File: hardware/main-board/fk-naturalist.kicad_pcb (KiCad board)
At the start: 2 copper layers, 91.8 x 37 mm, 128 parts, among them J1 Conn_01x07, J10 S2B-PH-SM4-TB, J11 RF-SMA-EDGE, J4 Conn_01x02, J5 Conn_01x03, J6 Conn_01x05, J7 CONN-HDR-2x5, J8 Conn_01x09, J9 MICRO-USB, M1 MOUNT_HOLE, M2 FIDUCIAL, M3 MOUNT_HOLE, M4 MOUNT_HOLE, M5 FIDUCIAL, M6 MOUNT_HOLE, M7 MICROSD, M8 FIDUCIAL, Q1 2N7002LT1G, Q2 2N7002LT1G, Q3 2N7002LT1G, Q4 2N7002LT1G, Q5 2N7002LT1G, SW1 SPNO, SW2 SPNO, U1 ATWINC1500-MR210PA, U10 FGPMMOPA6H, U103 BNO055, U11 MAX1704XX, U2 ATSAMD21G18A-AU, U4 24AA02E64, U5 S25FL116K0XMFI041, U6 BQ24074RGTT, U7 PCF8523, U8 MCP1700T-3302E/MB, U9 ISL8541x, Y1 FC-135, Y101 FC-135, Y2 FC-135

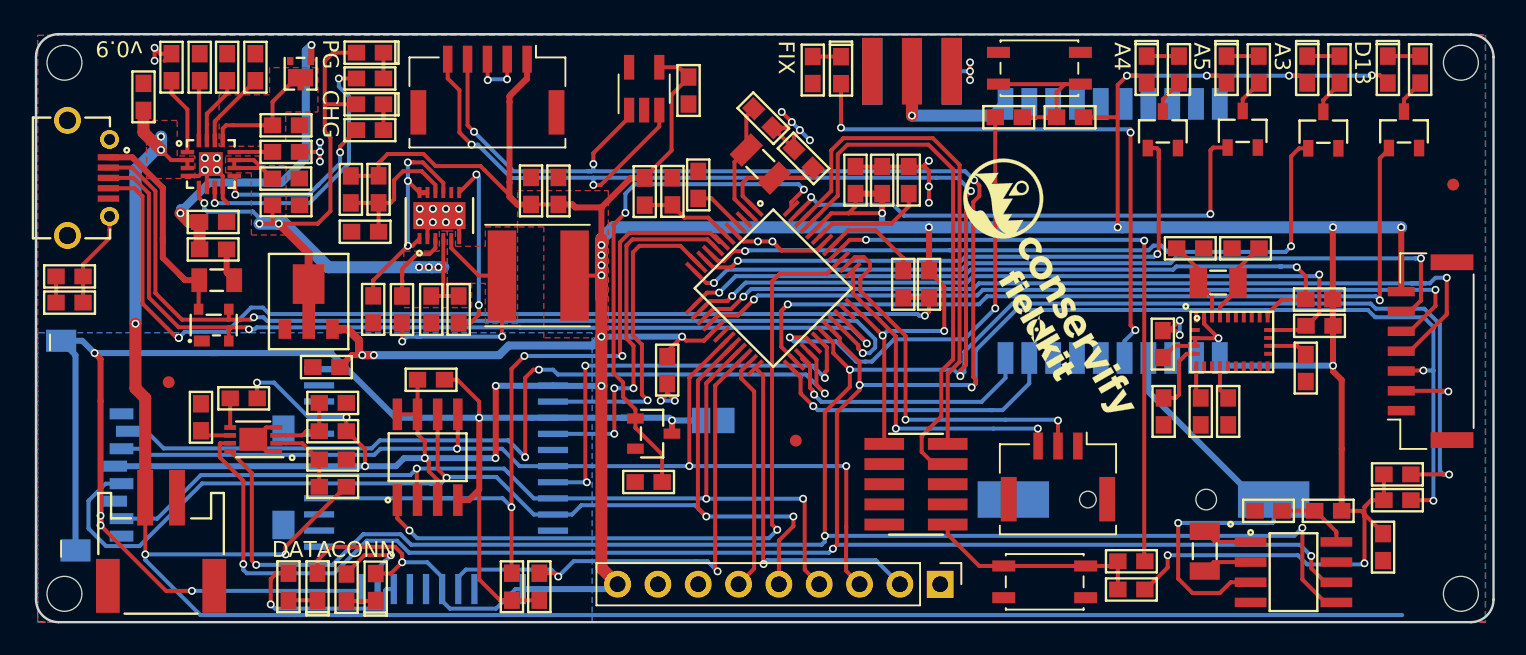
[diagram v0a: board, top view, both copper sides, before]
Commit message: Fix traces on MCU and via in pads on some ICs.
Replot with aux origin on drills.
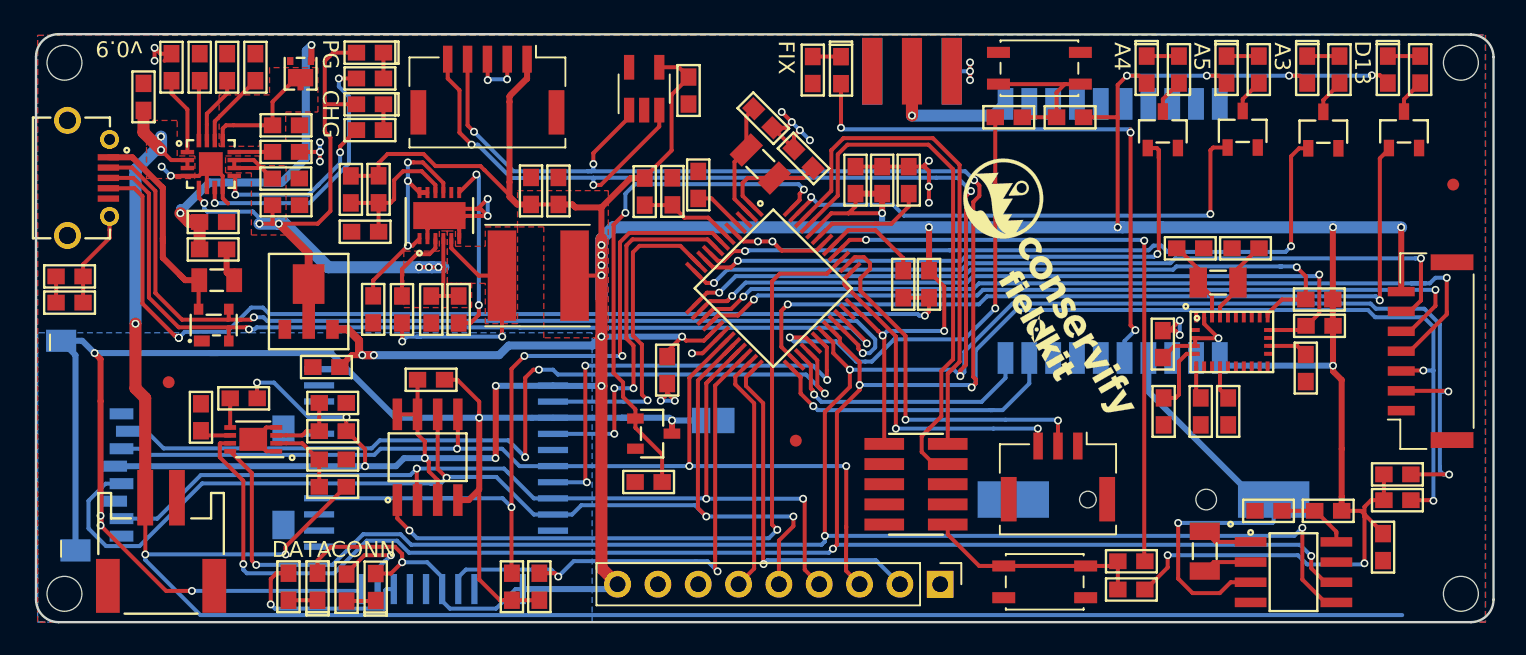
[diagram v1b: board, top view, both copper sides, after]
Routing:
- net GND: track 56.5 -> 66.7 mm, vias 35 -> 28

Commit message: Adding fiducials to the bottom.
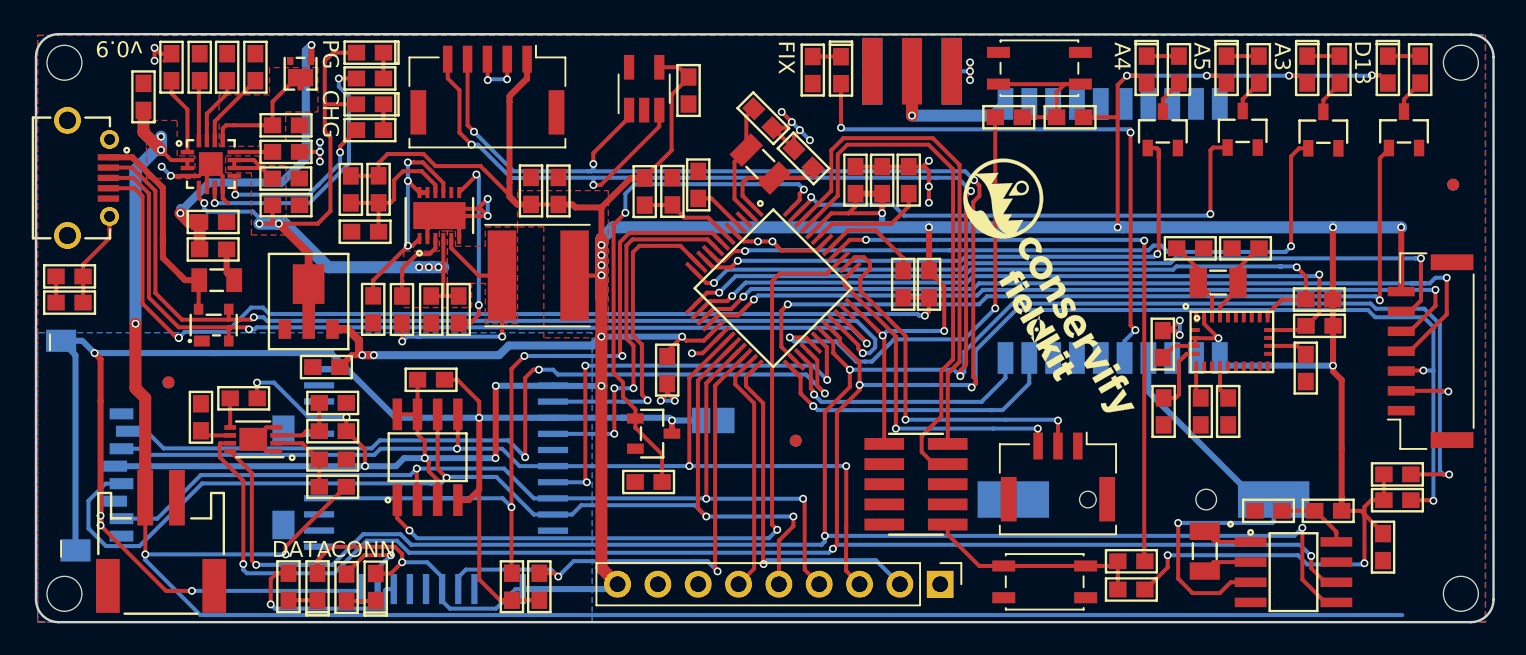
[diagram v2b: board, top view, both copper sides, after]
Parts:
- added M10: FIDUCIAL, Fiducials:Fiducial_0.75mm_Dia_1.5mm_Outer, B.Cu at (125.2, 135.4)
- added M11: FIDUCIAL, Fiducials:Fiducial_0.75mm_Dia_1.5mm_Outer, B.Cu at (85.7, 131.7)
- added M9: FIDUCIAL, Fiducials:Fiducial_0.75mm_Dia_1.5mm_Outer, B.Cu at (166.6, 119.3)
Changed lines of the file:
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@@
     (links 324)
     (no_connects 0)
-    (area 62.463333 91.834285 172.069744 151.864743)
+    (area 77.293399 109.703799 169.239001 146.887001)
     (thickness 1.6)
     (drawings 24)
     (tracks 1480)
     (zones 0)
-    (modules 128)
-    (nets 140)
+    (modules 131)
+    (nets 143)
   )
   (page A4)
@@
   )
   (layers
-    (0 F.Cu signal)
+    (0 F.Cu signal hide)
     (31 B.Cu signal)
     (32 B.Adhes user)
@@
   (net 138 "Net-(M5-Pad~)")
   (net 139 "Net-(M8-Pad~)")
+  (net 140 "Net-(M9-Pad~)")
+  (net 141 "Net-(M10-Pad~)")
+  (net 142 "Net-(M11-Pad~)")
   (net_class Default "This is the default net class."
     (clearance 0.1524)
@@
     (add_net "Net-(J9-Pad8)")
     (add_net "Net-(J9-Pad9)")
+    (add_net "Net-(M10-Pad~)")
+    (add_net "Net-(M11-Pad~)")
     (add_net "Net-(M2-Pad~)")
     (add_net "Net-(M5-Pad~)")
@@
     (add_net "Net-(M7-PadCD2)")
     (add_net "Net-(M8-Pad~)")
+    (add_net "Net-(M9-Pad~)")
     (add_net "Net-(Q1-Pad3)")
     (add_net "Net-(Q2-Pad3)")
@@
       (net 139 "Net-(M8-Pad~)") (solder_mask_margin 0.375) (clearance 0.375))
   )
+  (module Fiducials:Fiducial_0.75mm_Dia_1.5mm_Outer (layer B.Cu)
+    (at 166.61892 119.25808)
+    (descr "Circular Fiducial, 0.75mm bare copper top; 1.5mm keepout (Level B)")
+    (tags marker)
+    (attr virtual)
+    (fp_text reference M9 (at 0 2) (layer B.SilkS) hide
+      (effects (font (size 1 1) (thickness 0.15)) (justify mirror))
+    )
+    (fp_text value FIDUCIAL (at 0 -2) (layer B.Fab)
+      (effects (font (size 1 1) (thickness 0.15)) (justify mirror))
+    )
+    (fp_circle (center 0 0) (end 0.75 0) (layer B.Fab) (width 0.1))
+    (fp_text user %R (at 0 0) (layer B.Fab)
+      (effects (font (size 0.3 0.3) (thickness 0.05)) (justify mirror))
+    )
+    (fp_circle (center 0 0) (end 1 0) (layer B.CrtYd) (width 0.05))
+    (pad ~ smd circle (at 0 0) (size 0.75 0.75) (layers B.Cu B.Mask)
+      (net 140 "Net-(M9-Pad~)") (solder_mask_margin 0.375) (clearance 0.375))
+  )
+  (module Fiducials:Fiducial_0.75mm_Dia_1.5mm_Outer (layer B.Cu)
+    (at 125.21692 135.38708)
+    (descr "Circular Fiducial, 0.75mm bare copper top; 1.5mm keepout (Level B)")
+    (tags marker)
+    (attr virtual)
+    (fp_text reference M10 (at 0 2) (layer B.SilkS) hide
+      (effects (font (size 1 1) (thickness 0.15)) (justify mirror))
+    )
+    (fp_text value FIDUCIAL (at 0 -2) (layer B.Fab)
+      (effects (font (size 1 1) (thickness 0.15)) (justify mirror))
+    )
+    (fp_circle (center 0 0) (end 0.75 0) (layer B.Fab) (width 0.1))
+    (fp_text user %R (at 0 0) (layer B.Fab)
+      (effects (font (size 0.3 0.3) (thickness 0.05)) (justify mirror))
+    )
+    (fp_circle (center 0 0) (end 1 0) (layer B.CrtYd) (width 0.05))
+    (pad ~ smd circle (at 0 0) (size 0.75 0.75) (layers B.Cu B.Mask)
+      (net 141 "Net-(M10-Pad~)") (solder_mask_margin 0.375) (clearance 0.375))
+  )
+  (module Fiducials:Fiducial_0.75mm_Dia_1.5mm_Outer (layer B.Cu)
+    (at 85.70468 131.71932)
+    (descr "Circular Fiducial, 0.75mm bare copper top; 1.5mm keepout (Level B)")
+    (tags marker)
+    (attr virtual)
+    (fp_text reference M11 (at 0 2) (layer B.SilkS) hide
+      (effects (font (size 1 1) (thickness 0.15)) (justify mirror))
+    )
+    (fp_text value FIDUCIAL (at 0 -2) (layer B.Fab)
+      (effects (font (size 1 1) (thickness 0.15)) (justify mirror))
+    )
+    (fp_circle (center 0 0) (end 0.75 0) (layer B.Fab) (width 0.1))
+    (fp_text user %R (at 0 0) (layer B.Fab)
+      (effects (font (size 0.3 0.3) (thickness 0.05)) (justify mirror))
+    )
+    (fp_circle (center 0 0) (end 1 0) (layer B.CrtYd) (width 0.05))
+    (pad ~ smd circle (at 0 0) (size 0.75 0.75) (layers B.Cu B.Mask)
+      (net 142 "Net-(M11-Pad~)") (solder_mask_margin 0.375) (clearance 0.375))
+  )
   (gr_line (start 169.164 111.2266) (end 169.164 145.3896) (layer Edge.Cuts) (width 0.15))
   (gr_circle (center 93.4974 136.45429) (end 93.4474 136.40429) (layer F.SilkS) (width 0.3))
@@
     (connect_pads (clearance 0.2032))
     (min_thickness 0.2032)
-    (fill yes (arc_segments 32) (thermal_gap 0.254) (thermal_bridge_width 0.254))
+    (fill (arc_segments 32) (thermal_gap 0.254) (thermal_bridge_width 0.254))
     (polygon
       (pts
@@
     (connect_pads (clearance 0.2032))
     (min_thickness 0.2032)
-    (fill yes (arc_segments 32) (thermal_gap 0.254) (thermal_bridge_width 0.254))
+    (fill (arc_segments 32) (thermal_gap 0.254) (thermal_bridge_width 0.254))
     (polygon
       (pts
@@
     (connect_pads (clearance 0.2032))
     (min_thickness 0.2032)
-    (fill yes (arc_segments 32) (thermal_gap 0.254) (thermal_bridge_width 0.254))
+    (fill (arc_segments 32) (thermal_gap 0.254) (thermal_bridge_width 0.254))
     (polygon
       (pts
@@
     (connect_pads (clearance 0.2032))
     (min_thickness 0.2032)
-    (fill yes (arc_segments 32) (thermal_gap 0.254) (thermal_bridge_width 0.254))
+    (fill (arc_segments 32) (thermal_gap 0.254) (thermal_bridge_width 0.254))
     (polygon
       (pts
@@
     (connect_pads (clearance 0.2032))
     (min_thickness 0.2032)
-    (fill yes (arc_segments 32) (thermal_gap 0.254) (thermal_bridge_width 0.254))
+    (fill (arc_segments 32) (thermal_gap 0.254) (thermal_bridge_width 0.254))
     (polygon
       (pts
@@
     (connect_pads (clearance 0.2032))
     (min_thickness 0.2032)
-    (fill yes (arc_segments 32) (thermal_gap 0.254) (thermal_bridge_width 0.254))
+    (fill (arc_segments 32) (thermal_gap 0.254) (thermal_bridge_width 0.254))
     (polygon
       (pts
@@
     (connect_pads (clearance 0.2032))
     (min_thickness 0.2032)
-    (fill yes (arc_segments 32) (thermal_gap 0.254) (thermal_bridge_width 0.254))
+    (fill (arc_segments 32) (thermal_gap 0.254) (thermal_bridge_width 0.254))
     (polygon
       (pts
@@
     (connect_pads (clearance 0.2032))
     (min_thickness 0.2032)
-    (fill yes (arc_segments 32) (thermal_gap 0.254) (thermal_bridge_width 0.254))
+    (fill (arc_segments 32) (thermal_gap 0.254) (thermal_bridge_width 0.254))
     (polygon
       (pts
@@
     (connect_pads (clearance 0.2032))
     (min_thickness 0.254)
-    (fill yes (arc_segments 16) (thermal_gap 0.508) (thermal_bridge_width 0.508))
+    (fill (arc_segments 16) (thermal_gap 0.508) (thermal_bridge_width 0.508))
     (polygon
       (pts
